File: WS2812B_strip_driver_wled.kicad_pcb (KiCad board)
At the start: 2 copper layers, 112.9 x 106.2 mm, 115 parts, among them J1 CH_1, J2 CH_2, J3 CH_3, J4 CH_4, J5 PWR_IN, J6 uPhone, J8 USB_C_Receptacle_USB2.0_16P, K1 RELAY_1, K2 RELAY_2, K3 RELAY_3, K4 RELAY_4, Q1 SS8050, Q2 SS8050, Q3 SS8050, Q4 SS8050, Q5 SS8050, Q6 SS8050, SW1 SW_EN, SW2 SW_IO0, U1 ESP32-WROOM-32E, U2 AMS1117-3.3, U3 CP2102N-Axx-xQFN28

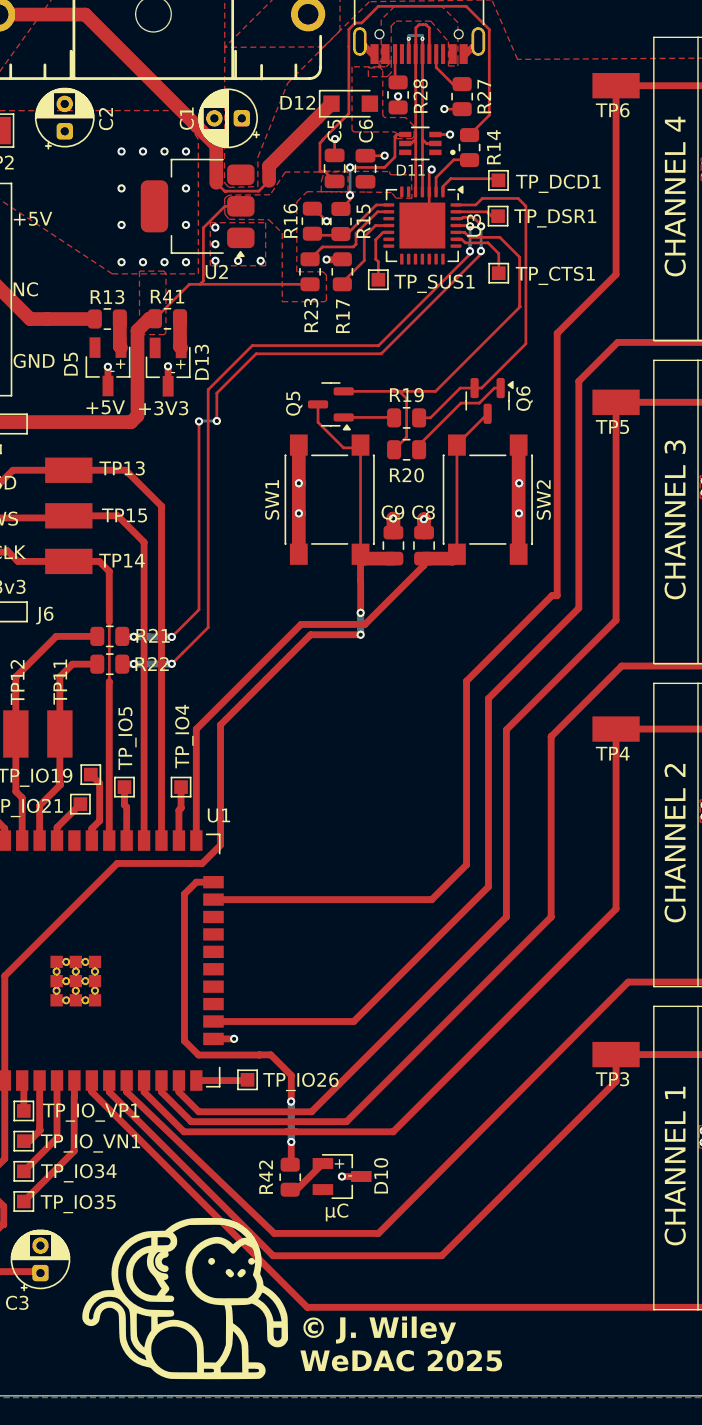
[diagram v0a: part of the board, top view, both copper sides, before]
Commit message: added btn labels, moved logo
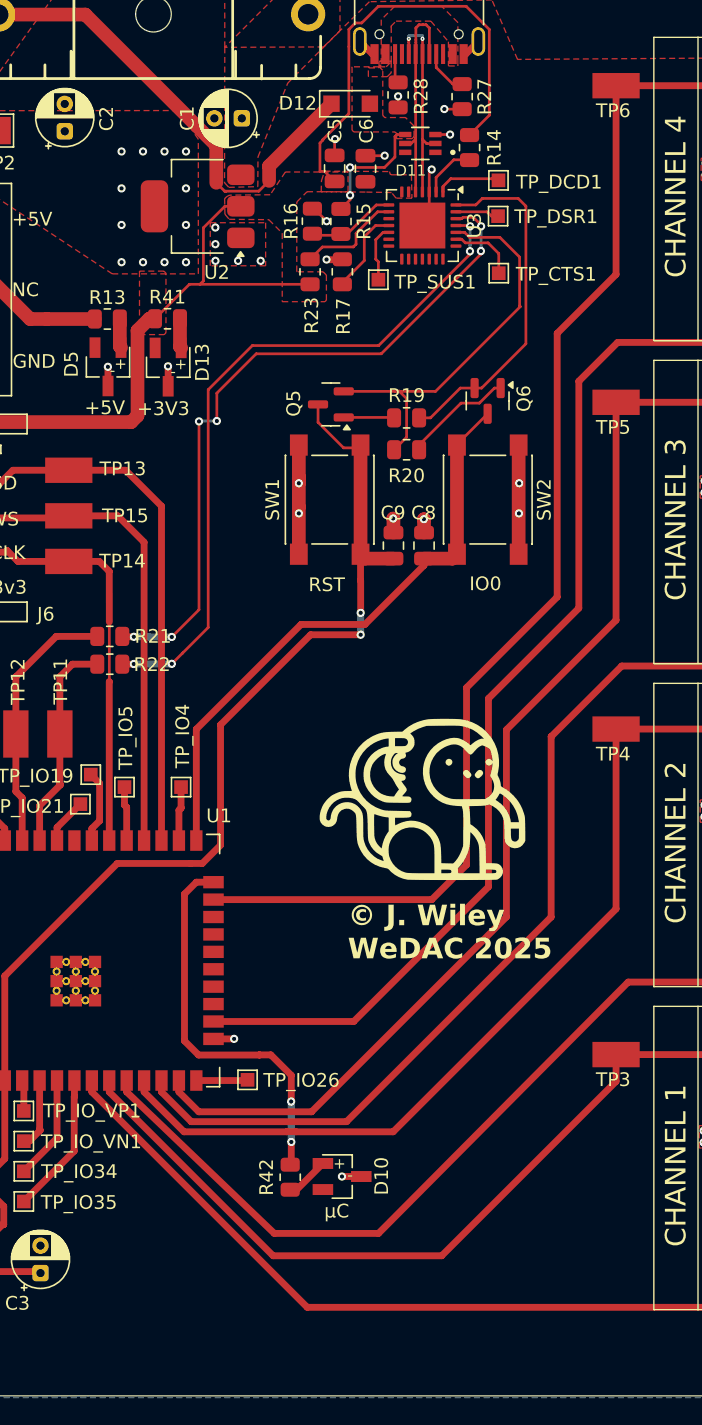
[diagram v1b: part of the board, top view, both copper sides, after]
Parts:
- moved G*** 40.3 mm to (54.1, 136.6)
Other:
- board text added: "IO0"
- board text added: "RST"

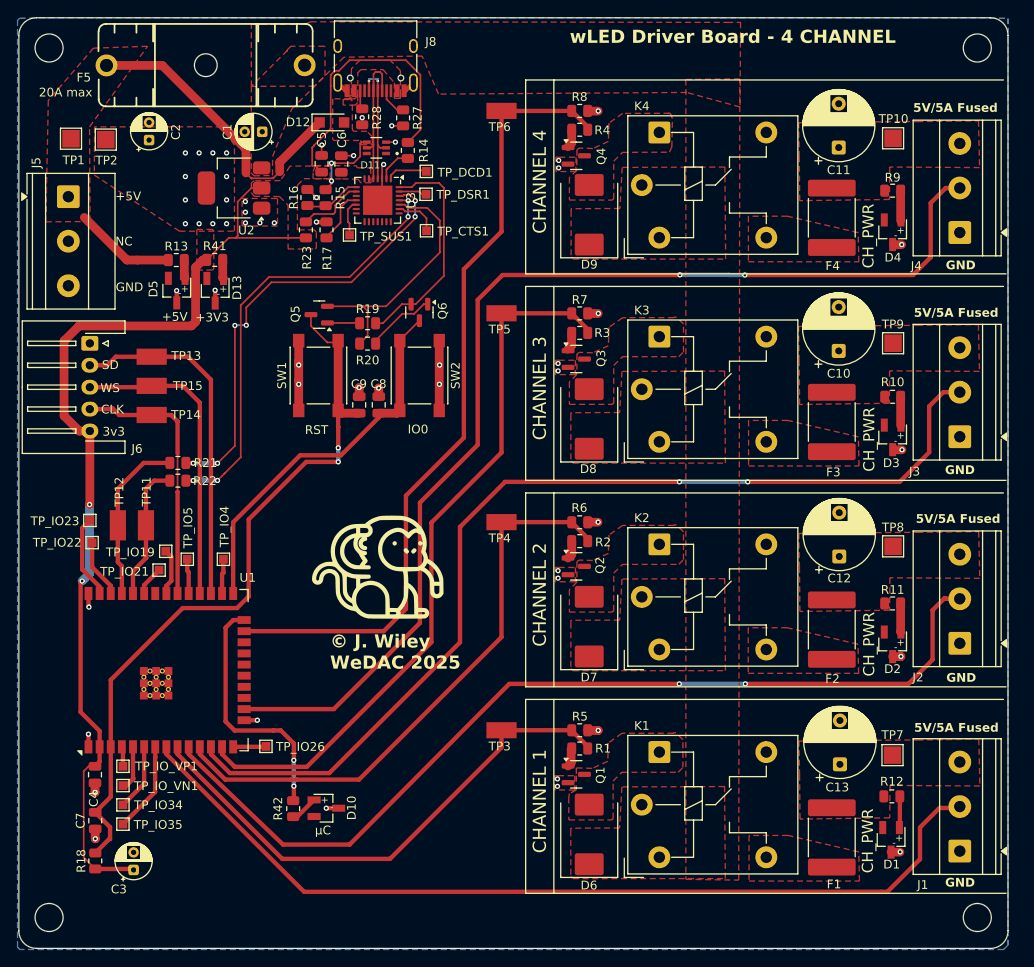
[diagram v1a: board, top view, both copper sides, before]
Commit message: More silkscreen improvements/additions
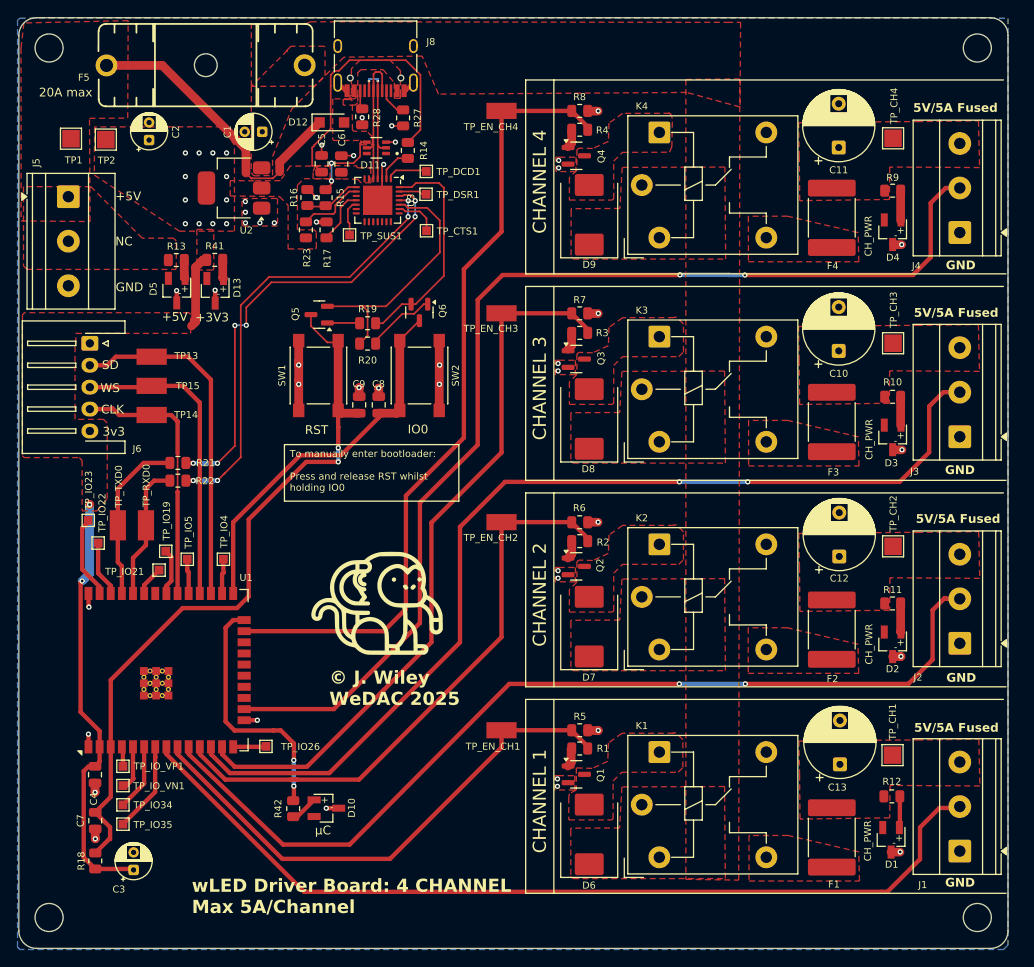
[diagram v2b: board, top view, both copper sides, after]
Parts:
- moved G*** 4.13 mm to (54.0, 140.7)
- moved TP_IO22 0.69 mm to (22.2, 133.9)
- moved TP_IO23 0.18 mm to (21.1, 131.3)
- renumbered TP7 to TP_CH1, TP8 to TP_CH2, TP9 to TP_CH3, TP10 to TP_CH4, TP3 to TP_EN_CH1, TP4 to TP_EN_CH2, TP5 to TP_EN_CH3, TP6 to TP_EN_CH4, TP11 to TP_RXD0, TP12 to TP_TXD0
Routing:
- net +3V3: track 145.7 -> 89.9 mm
- net +5V: track 46.8 -> 35.2 mm
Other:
- board text added: "To manually enter bootloader: Press and release RST whilst holding IO0"
- board text added: "wLED Driver Board: 4 CHANNEL Max 5A/Channel"
- board text removed: "wLED Driver Board - 4 CHANNEL"

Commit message: reordered channels, renamed TP's, moved uC good led
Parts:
- G***: footprint CUSTOM_LOGOS:Monkey_15x15 -> CUSTOM_LOGOS:Monkey_25x25
- moved TP_EN_CH4 70.7 mm to (68.2, 155.3), turned to 0 degrees
- moved D4 70.7 mm to (112.8, 169.1)
- moved K4 70.7 mm to (86.2, 157.7)
- moved C11 70.7 mm to (106.7, 159.5)
- moved D9 70.7 mm to (78.2, 167.1)
- moved F4 70.7 mm to (105.9, 167.5)
- moved J4 70.7 mm to (120.5, 169.2)
- moved Q4 70.7 mm to (76.7, 160.4)
- moved R4 70.7 mm to (77.1, 157.4)
- moved R8 70.7 mm to (77.1, 155.3)
- moved R9 70.7 mm to (112.8, 164.4)
- moved TP_EN_CH1 70.7 mm to (68.2, 84.6), turned to 0 degrees
- moved TP_CH1 70.5 mm to (112.7, 87.6), turned to 0 degrees
- moved D1 70.3 mm to (112.4, 97.5)
- moved D6 70.3 mm to (78.0, 96.8)
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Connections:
- U1 pad 10: CH_2_DAT -> CH_3_DAT
- U1 pad 11: CH_2_EN -> CH_3_EN
- U1 pad 12: CH_3_DAT -> CH_2_DAT
- U1 pad 13: CH_3_EN -> CH_2_EN
- U1 pad 16: CH_4_DAT -> CH_1_DAT
- U1 pad 23: CH_4_EN -> CH_1_EN
- U1 pad 8: CH_1_DAT -> CH_4_DAT
- U1 pad 9: CH_1_EN -> CH_4_EN
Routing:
- net CH_1_EN: track 60.8 -> 91.7 mm
- net CH_4_EN: track 91.8 -> 60.9 mm
- net uC_GOOD: track 28.6 -> 4.13 mm, vias 2 -> 0
- net CH_4_DAT: track 127.7 -> 104.0 mm, vias 2 -> 0
- net CH_1_DAT: track 104.0 -> 127.7 mm, vias 0 -> 2
- net CH_3_EN: track 83.0 -> 67.3 mm
- net CH_2_EN: track 67.2 -> 82.9 mm
- net CH_3_DAT: track 116.0 -> 108.0 mm
- net CH_2_DAT: track 108.0 -> 116.0 mm
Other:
- board text added: "5V"
- board text added: "μPhone"
- board text removed: "5V/5A Fused"

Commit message: added 0402 zero-ohm for solder-blob jumpering the channels. Even better silkscreen
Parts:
- added R24: 0, Resistor_SMD:R_0402_1005Metric, F.Cu at (68.2, 95.9)
- added R25: 0, Resistor_SMD:R_0402_1005Metric, F.Cu at (68.2, 119.4)
- added R26: 0, Resistor_SMD:R_0402_1005Metric, F.Cu at (68.2, 142.8)
- added R29: 0, Resistor_SMD:R_0402_1005Metric, F.Cu at (68.2, 166.6)
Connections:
- R1 pad 1: CH_1_EN -> Net-(R1-Pad1)
- R2 pad 1: CH_2_EN -> Net-(R2-Pad1)
- R3 pad 1: CH_3_EN -> Net-(R26-Pad2)
- R4 pad 1: CH_4_EN -> Net-(R29-Pad2)
- R5 pad 1: CH_1_EN -> Net-(R1-Pad1)
- R6 pad 1: CH_2_EN -> Net-(R2-Pad1)
- R7 pad 1: CH_3_EN -> Net-(R26-Pad2)
- R8 pad 2: CH_4_EN -> Net-(R29-Pad2)
- TP_EN_CH1 pad 1: CH_1_EN -> Net-(R1-Pad1)
- TP_EN_CH2 pad 1: CH_2_EN -> Net-(R2-Pad1)
- TP_EN_CH3 pad 1: CH_3_EN -> Net-(R26-Pad2)
- TP_EN_CH4 pad 1: CH_4_EN -> Net-(R29-Pad2)
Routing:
- net CH_2_EN: track 82.9 -> 59.8 mm
- net CH_3_EN: track 67.3 -> 44.5 mm
- net CH_1_EN: track 91.7 -> 69.0 mm
- net Net-(R2-Pad1): track 0.00 -> 22.1 mm
- net Net-(R26-Pad2): track 0.00 -> 21.8 mm
- net Net-(R29-Pad2): track 0.00 -> 21.7 mm
- net Net-(R1-Pad1): track 0.00 -> 21.7 mm
- net CH_4_EN: track 60.9 -> 44.4 mm
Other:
- board text added: "INMP441 μPhone"
- board text added: "WLED Multirelay Driver Board: 4 Channel: Max 5A/Channel Audioreactive: INMP441 I2S microphone"
- board text removed: "wLED Driver Board: 4 CHANNEL Max 5A/Channel"
- board text removed: "μPhone"

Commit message: added JLCJLCJLCJLC to silkscreen for manual positioning under chip
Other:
- board text added: "JLCJLCJLCJLC"
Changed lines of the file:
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@@
+		)
+	)
+	(gr_text "JLCJLCJLCJLC"
+		(at 24.03 144.6 0)
+		(layer "F.SilkS")
+		(effects
+			(font
+				(size 1 1)
+				(thickness 0.1)
+			)
+			(justify left bottom)
 		)
 	)

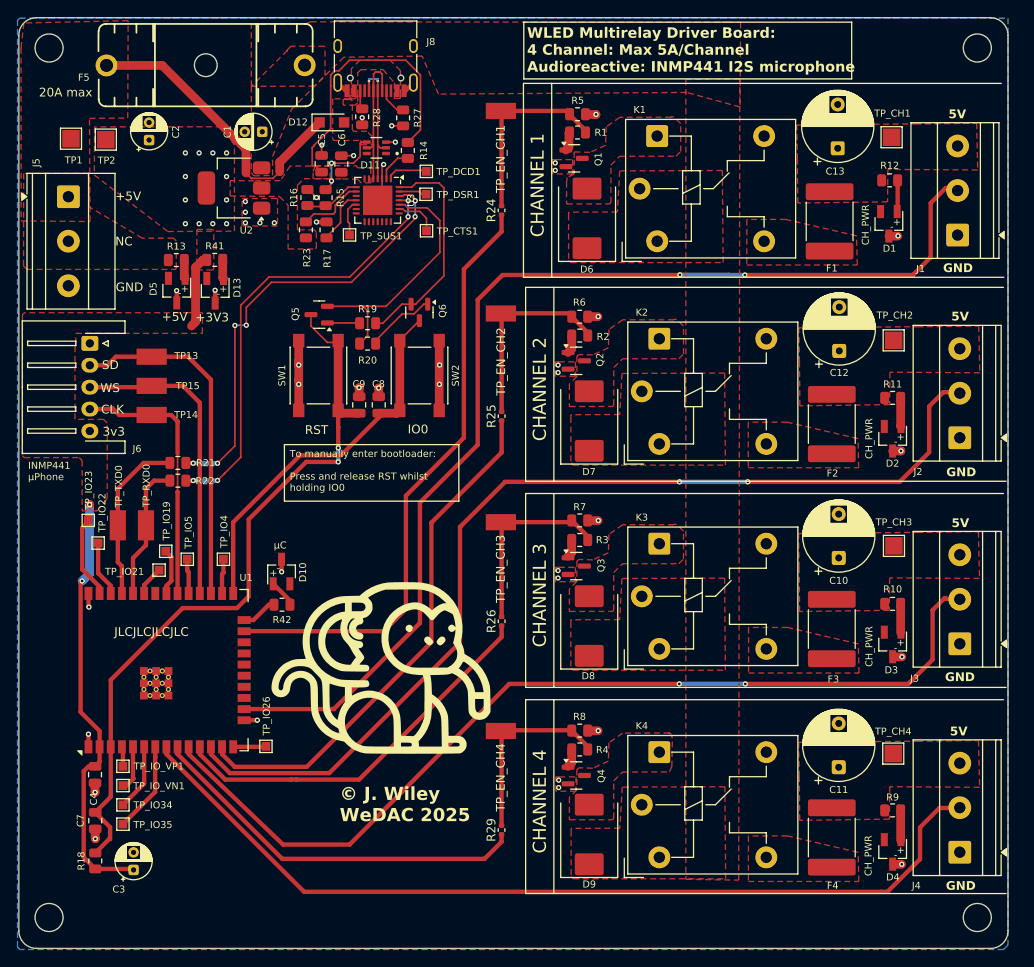
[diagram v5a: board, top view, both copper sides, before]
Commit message: more silkscreen updates, moved pwr_in connnector slightly to allow room for better labelling
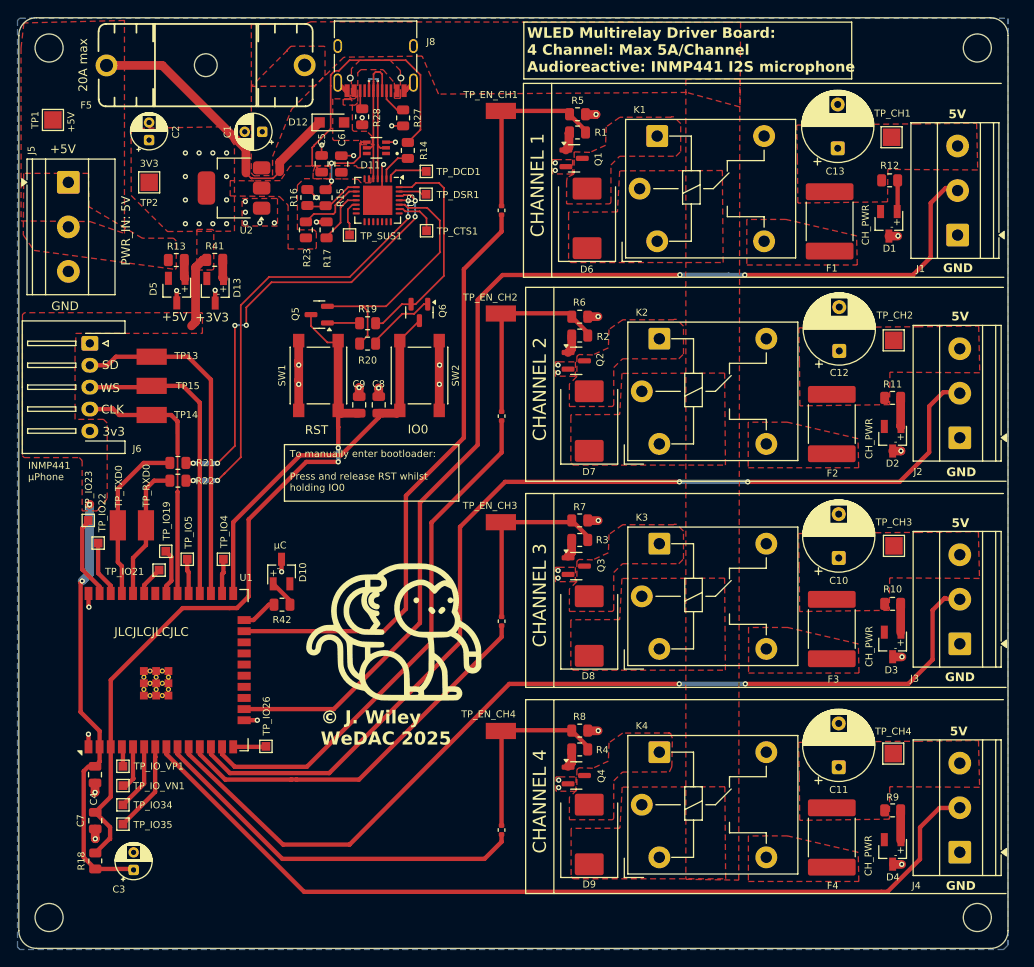
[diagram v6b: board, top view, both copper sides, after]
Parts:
- G***: footprint CUSTOM_LOGOS:Monkey_25x25 -> CUSTOM_LOGOS:Monkey_20x20
- moved TP2 6.95 mm to (28.0, 92.7)
- moved G*** 4.35 mm to (55.9, 144.0)
- moved TP1 2.97 mm to (17.0, 85.6)
- moved J5 1.64 mm to (18.8, 92.7)
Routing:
- net +5V: track 35.2 -> 34.5 mm
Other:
- board text added: "3V3"
- board text added: "PWR_IN: 5V"
- board text removed: "NC"

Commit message: moved testpoints, aligned channel 1, better silkscreen
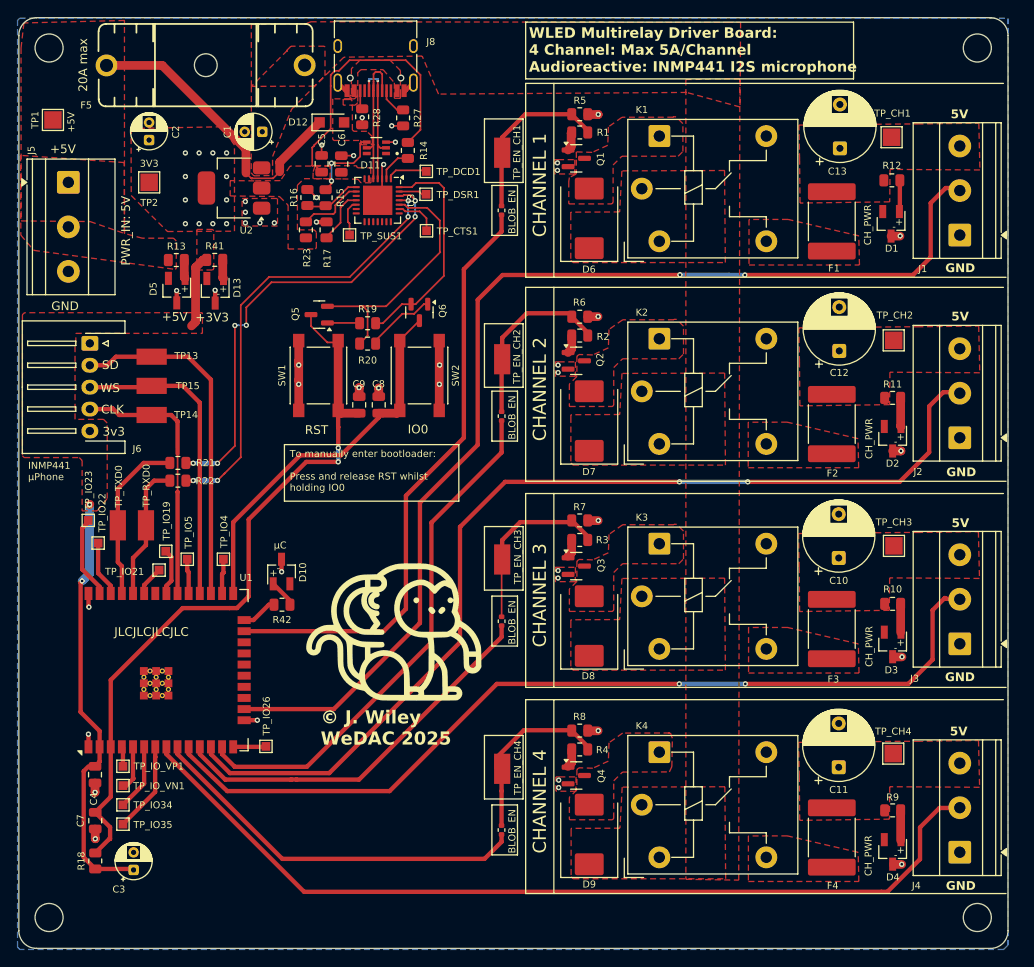
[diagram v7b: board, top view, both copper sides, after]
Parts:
- moved TP_EN_CH2 5.19 mm to (68.3, 112.9), turned to 90 degrees
- moved TP_EN_CH1 4.74 mm to (68.3, 89.3), turned to 90 degrees
- moved TP_EN_CH4 4.29 mm to (68.3, 159.6), turned to 90 degrees
- moved TP_EN_CH3 4.23 mm to (68.3, 135.7), turned to 90 degrees
- moved C13 0.25 mm to (106.8, 88.8)
- moved D1 0.25 mm to (112.7, 97.5)
- moved D6 0.25 mm to (78.2, 96.8)
- moved F1 0.25 mm to (105.9, 97.2)
- moved J1 0.25 mm to (120.5, 98.7)
- moved K1 0.25 mm to (86.2, 87.4)
- moved Q1 0.25 mm to (76.7, 90.0)
- moved R1 0.25 mm to (77.1, 87.0)
- moved R12 0.25 mm to (112.7, 92.5)
- moved R5 0.25 mm to (77.1, 85.0)
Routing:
- net CH_3_DAT: track 108.0 -> 103.0 mm
- net Net-(R1-Pad1): track 21.7 -> 19.7 mm
- net Net-(R2-Pad1): track 22.1 -> 20.5 mm
- net Net-(R26-Pad2): track 21.8 -> 20.5 mm
- net Net-(R29-Pad2): track 21.7 -> 20.7 mm
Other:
- board text added: "BLOB_EN"
